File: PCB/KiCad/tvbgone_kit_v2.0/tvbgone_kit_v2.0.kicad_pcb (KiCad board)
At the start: 2 copper layers, 59.9 x 49.3 mm, 25 parts, among them Q1 IRLU024NPBF, U1 TSOP38238

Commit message: new IR LED resistors, updated BOM & assembly
* After testing, R1-R4 were reduced to 1 Ohm to maximize range of IR LEDs.
* Updated BOM.
* Put Gerber files in their own subdirectory.
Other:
- board text added: "1"
- board text removed: "3.3"
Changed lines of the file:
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@@
 		(filling no)
 		(pcbplotparams
-			(layerselection 0x00000000_00000000_55555555_57557573)
+			(layerselection 0x00000000_00000000_55555555_575555ff)
 			(plot_on_all_layers_selection 0x00000000_00000000_00000000_00000000)
 			(disableapertmacros no)
-			(usegerberextensions no)
-			(usegerberattributes yes)
-			(usegerberadvancedattributes yes)
-			(creategerberjobfile yes)
+			(usegerberextensions yes)
+			(usegerberattributes no)
+			(usegerberadvancedattributes no)
+			(creategerberjobfile no)
 			(dashed_line_dash_ratio 12)
 			(dashed_line_gap_ratio 3)
@@
 			(drillshape 0)
 			(scaleselection 1)
-			(outputdirectory "")
+			(outputdirectory "Gerbers/")
 		)
 	)
@@
 		)
 	)
-	(gr_text "3.3"
+	(gr_text "1"
 		(at 126.85 109.95 90)
 		(layer "B.SilkS")
@@
 		)
 	)
-	(gr_text "3.3"
+	(gr_text "1"
 		(at 133.25 109.95 90)
 		(layer "B.SilkS")
@@
 		)
 	)
-	(gr_text "3.3"
+	(gr_text "1"
 		(at 139.4 109.95 90)
 		(layer "B.SilkS")
@@
 		)
 	)
-	(gr_text "3.3"
+	(gr_text "1"
 		(at 145.55 109.95 90)
 		(layer "B.SilkS")

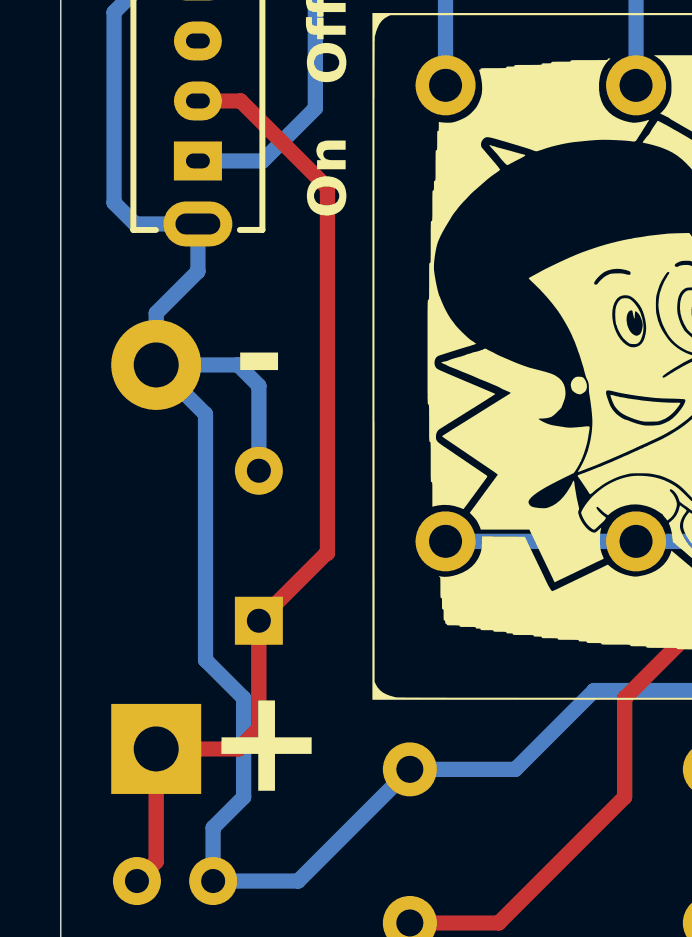
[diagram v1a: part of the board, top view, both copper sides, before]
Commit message: Change C2 to 0.1" lead-spacing
Change C2 to 0.1" lead-spacing
C2 part number changed from Panasonic ECE-A0JKA331Q to Panasonic ECE-A0JKA331
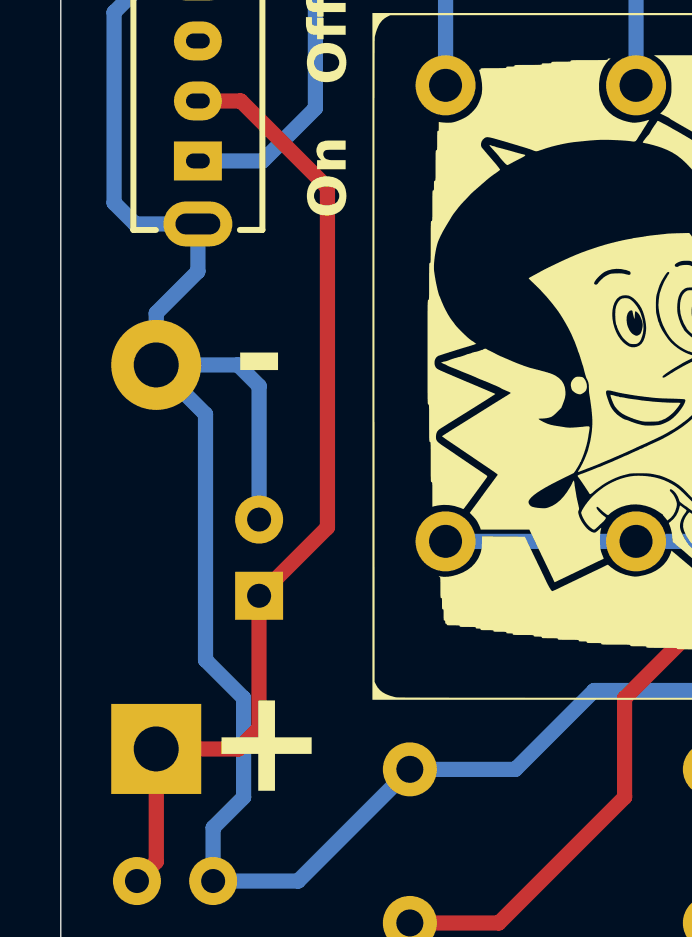
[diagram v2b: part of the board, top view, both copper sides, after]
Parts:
- R1, R2, R3, R4: value 120 -> 1
- moved C2 0.40 mm to (120.2, 118.0)
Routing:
- net GND: track 196.7 -> 198.4 mm
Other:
- board text added: "kit V2.0 r3"
- board text removed: "kit V2.0 r2"
